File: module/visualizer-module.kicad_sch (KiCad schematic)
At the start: 13 parts, among them J1 USB4110GFA

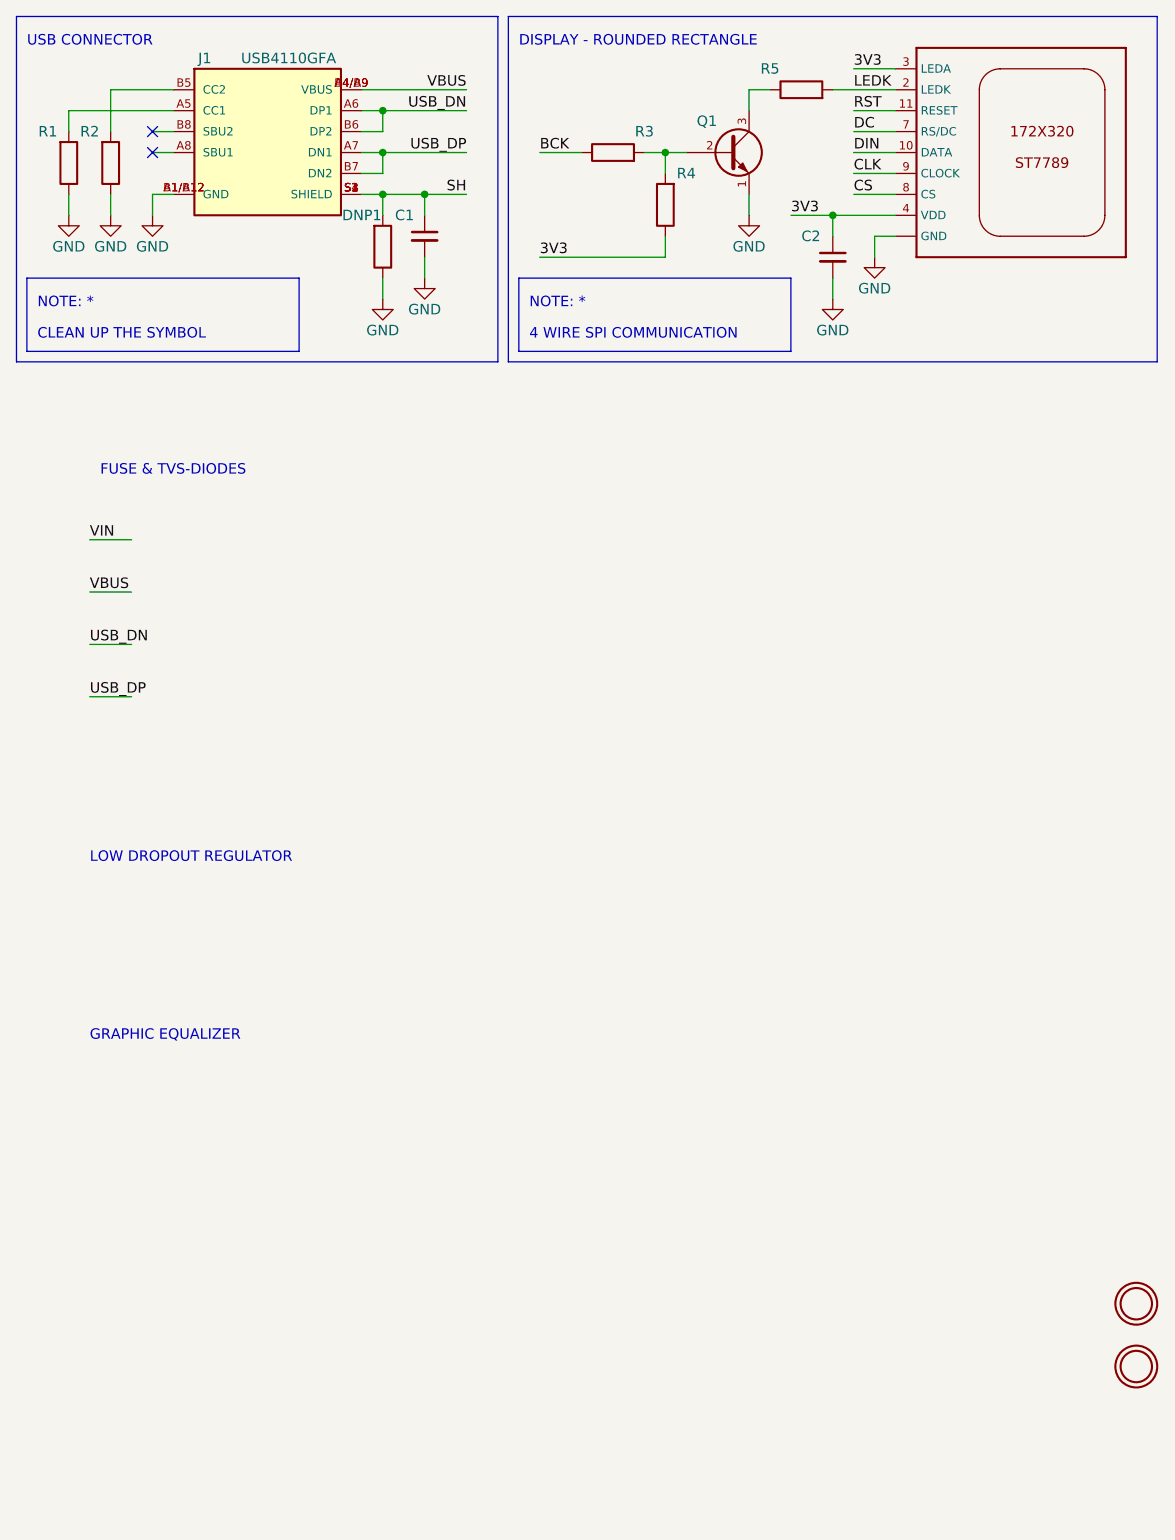
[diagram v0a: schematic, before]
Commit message: Added more components and edited schematic
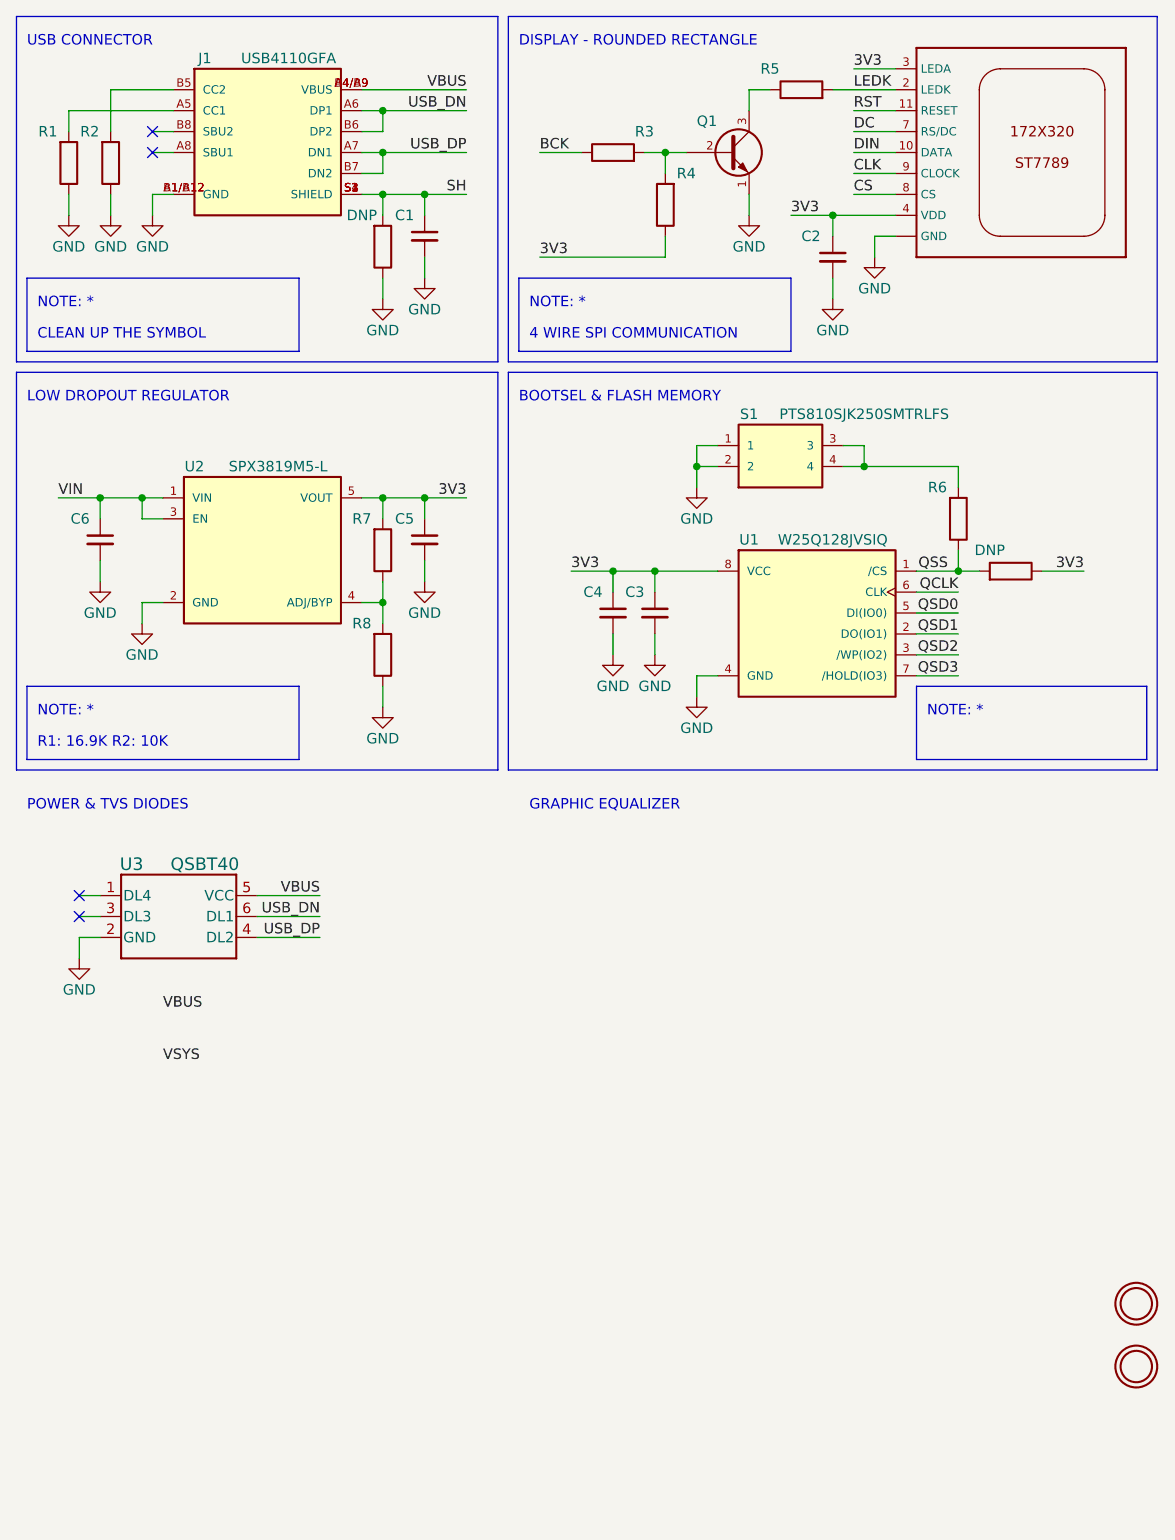
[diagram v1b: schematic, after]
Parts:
- added C3, C4, C5, C6: 0.1uF_0603_16V, Capacitor_SMD:C_0603_1608Metric, symbol PCM_4ms_Capacitor:0.1uF_0603_16V
- added DNP, R6, R7, R8: 10K_0603, PCM_Resistor_SMD_AKL:R_0201_0603Metric, symbol PCM_4ms_Resistor:0R_0603
- added S1: PTS810SJK250SMTRLFS, symbol PTS810SJK250SMTRLFS:PTS810SJK250SMTRLFS
- added U1: W25Q128JVSIQ, symbol W25Q128JVPIM:W25Q128JVSIQ
- added U2: SPX3819M5-L, symbol SPX3819M5-L:SPX3819M5-L
- added U3: QSBT40, symbol QSBT40-7-F:QSBT40-7-F
- renumbered DNP1 to DNP
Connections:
- net 3V3: now also C3.1, C4.1, C5.1, DNP.1, R7.2, U1.8 (VCC), U2.5 (VOUT)
- net GND: now also C3.2, C4.2, C5.2, C6.2, R8.1, S1.1, S1.2, U1.4 (GND), U2.2 (GND), U3.2 (GND)
- net USB_DN: now also U3.6 (DL1)
- net USB_DP: now also U3.4 (DL2)
- net VBUS: now also U3.5 (VCC)
- net VIN: now also C6.1, U2.1 (VIN), U2.3 (EN)
- new net: R6.2, S1.3, S1.4
- new net: R7.1, R8.2, U2.4 (ADJ/BYP)
- new net QCLK: U1.6 (CLK)
- new net QSD0: U1.5 (DI(IO0))
- new net QSD1: U1.2 (DO(IO1))
- new net QSD2: U1.3 (/WP(IO2))
- new net QSD3: U1.7 (/HOLD(IO3))
- new net QSS: DNP.2, R6.1, U1.1 (/CS)
- no-connect marks 2 -> 4
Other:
- note added: "BOOTSEL & FLASH MEMORY"
- note added: "POWER & TVS DIODES"
- note added: "R1: 16.9K R2: 10K"
- note removed: "FUSE & TVS-DIODES"

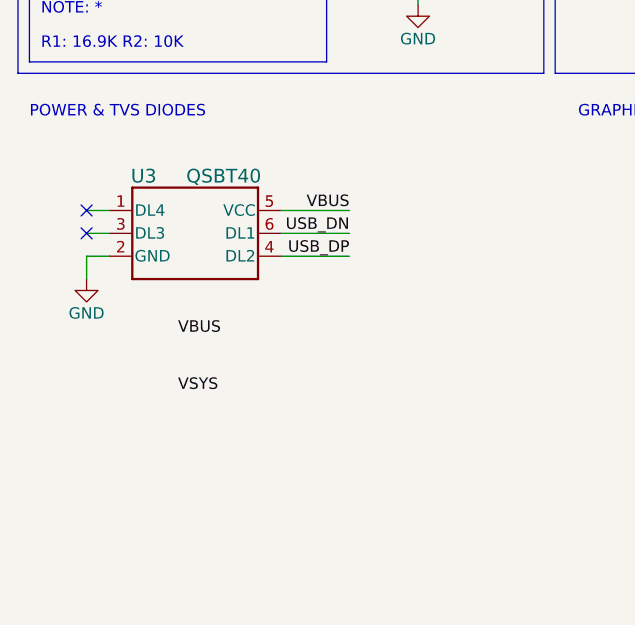
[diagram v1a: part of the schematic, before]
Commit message: Added and edited some components + schematic update
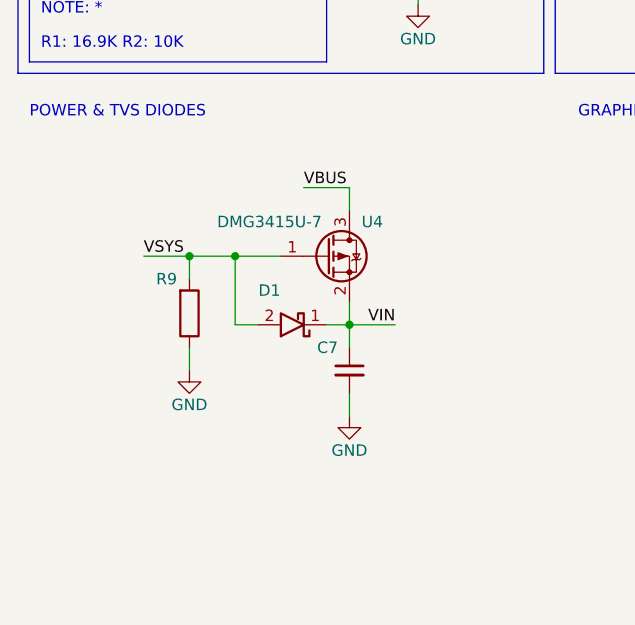
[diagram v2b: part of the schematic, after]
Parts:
- removed U3: QSBT40, symbol QSBT40-7-F:QSBT40-7-F
- added C7: 0.1uF_0603_16V, Capacitor_SMD:C_0603_1608Metric, symbol PCM_4ms_Capacitor:0.1uF_0603_16V
- added D1: SS14, symbol SS14:SS14
- added R9: 10K_0603, PCM_Resistor_SMD_AKL:R_0201_0603Metric, symbol PCM_4ms_Resistor:0R_0603
- added U4: DMG3415U-7, symbol DMG3415U-7:DMG3415U-7
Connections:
- net GND: now also C7.2, R9.1
- net VBUS: now also U4.3
- net VIN: now also C7.1, D1.1, U4.2
- net VSYS: now also D1.2, R9.2, U4.1
- no-connect marks 4 -> 2

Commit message: kicad_sch.lck added to .gitignore
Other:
- note added: "AUTOMATIC POWER SELECTION"
- note added: "ESD PROTECTION"
- note added: "ROTATE THE SYMBOL"
- note removed: "POWER & TVS DIODES"
- moved on the sheet: C7, D1, R9, U4

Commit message: Updated symbol and attached some models to some of the components
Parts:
- removed DNP: 10K_0603, PCM_Resistor_SMD_AKL:R_0201_0603Metric, symbol PCM_4ms_Resistor:0R_0603
- added DNP2: 10K_0603, PCM_Resistor_SMD_AKL:R_0201_0603Metric, symbol PCM_4ms_Resistor:0R_0603
- D1: footprint (none) -> footprints:SS14
- Q1: footprint (none) -> footprints:S8050
- S1: footprint (none) -> footprints:PTS810SJG250SMTRLFS
- U1: footprint (none) -> footprints:W25Q128JVPIM
- U2: footprint (none) -> footprints:SPX3819M5-L
- U4: footprint (none) -> footprints:DMG3415U-7
- renumbered DNP to DNP1
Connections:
- net 3V3: now also DNP2.1
- net QSD0: now also U1.2 (DO(IO1)); no longer U1.5 (DI(IO0))
- net QSD1: now also U1.5 (DI(IO0)); no longer U1.2 (DO(IO1))
- net QSS: now also DNP2.2
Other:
- note added: "USE SOMETHING ELSE INSTEAD OF THESE BOXES SURROUNDING THE CIRCUITS"
- note removed: "ESD PROTECTION"
- note removed: "ROTATE THE SYMBOL"
- moved on the sheet: U1
